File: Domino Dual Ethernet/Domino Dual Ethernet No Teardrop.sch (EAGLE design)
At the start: 21 parts, among them J1 MH10-1, J2 B50(27-51)FP4-151-A613-B12, J3 B50(27-51)FP4-151-A613-B12, J4 FR04-2, J5 FR04-1

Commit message: Changed copyright
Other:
- note added: "The Domino Team may make changes to specifications and product"
- note added: "© 2014, The Domino Team All rights reserved."
- note removed: "Michel Stempin may make changes to specifications and product"
- note removed: "© 2014, Michel Stempin All rights reserved."
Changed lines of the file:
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@@
 <text x="302.26" y="12.7" size="0.8128" layer="94">Reference designs are provided "AS IS" and "WITH ALL FAULTS".</text>
 <text x="302.26" y="10.16" size="0.8128" layer="94">regarding this product, including but not limited to, any implied warranties of</text>
-<text x="302.26" y="6.35" size="0.8128" layer="94">Michel Stempin may make changes to specifications and product </text>
+<text x="302.26" y="6.35" size="0.8128" layer="94">The Domino Team may make changes to specifications and product </text>
 <text x="302.26" y="11.43" size="0.8128" layer="94">Global Marine Networks disclaims all other warranties express or implied, </text>
 <text x="302.26" y="8.89" size="0.8128" layer="94">merchantibility or fitness for any particular application.</text>
@@
 <text x="256.54" y="7.62" size="1.778" layer="94" align="center">Domino
 Qi</text>
-<text x="345.44" y="20.32" size="1.27" layer="94">© 2014, Michel Stempin
+<text x="345.44" y="20.32" size="1.27" layer="94">© 2014, The Domino Team
 All rights reserved.</text>
 <text x="379.222" y="5.334" size="1.778" layer="94">&gt;REV</text>

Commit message: Domino tile Dual Ethernet Revision B
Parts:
- removed J4: FR04-2, Domino:FR04-2
- removed J5: FR04-1, Domino:FR04-1
- added D1: BLUE, Domino:LED_0603
- added D2: WHITE, Domino:LED_0603
- added D3, D4, D5, D6: GREEN, Domino:LED_0603
- added D7: RED, Domino:LED_0603
- added D8: ORANGE, Domino:LED_0603
- added D9: YELLOW, Domino:LED_0603
- added R10, R11, R12, R13, R15: 270R, Domino:RES_0603
- added R14, R16: 150R, Domino:RES_0603
- added R17, R18: 330R, Domino:RES_0603
- added R9: 49R9, Domino:RES_0402
- C1: device Domino:CAP_1210 -> Domino:CAP_1206
- J1: value MH10-1 -> B59(57-02)F4-03-1212-C12; device Domino:MH10-1 -> Domino:B59(57-02)F4-03-1212-C12; PARTNO MH10-1-0.1 -> B59(57-02)F4-03-1212-C12
- J2, J3: value B50(27-51)FP4-151-A613-B12 -> MH18-1; device Domino:B50(27-51)FP4-151-A613-B12 -> Domino:MH18-1; PARTNO B50(27-51)FP4-151-A613-B12 -> MH18-1-0.1
- R1: value 49R9 -> 330R; device Domino:RES_0402 -> Domino:RES_0603; PARTNO R0402_49R9_1%_62.5mW -> R0603_330R_5%_125mW; TOL 1% -> 5%
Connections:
- removed net P0_LED_L_A: J2.13, J4.8
- removed net P0_LED_L_C: J2.14, J4.7
- removed net P0_LED_R_A: J2.11, J4.4
- removed net P0_LED_R_C: J2.12, J4.3
- removed net P4_LED_L_A: J3.13, J4.6
- removed net P4_LED_L_C: J3.14, J4.5
- removed net P4_LED_R_A: J3.11, J4.2
- removed net P4_LED_R_C: J3.12, J4.1
- removed net VC12: J3.9, J5.3
- removed net VC36: J3.10, J5.4
- removed net VC45: J3.4, J5.1
- removed net VC78: J3.5, J5.2
- new net +3V3: D7.A, D8.A, D9.A, J1.UL2, J2.8, R1.2
- new net LAN1_LED: D3.A, R12.2
- new net LAN2_LED: D4.A, R13.2
- new net LAN3_LED: D5.A, J1.DL2, R14.2
- new net LAN4_LED: D6.A, R15.2
- new net LED0: J2.9, R10.1
- new net LED1: J2.10, R11.1
- new net LED2: J2.11, R12.1
- new net LED3: J2.12, R13.1
- new net LED4: J2.13, R14.1
- new net LED5: J2.14, R15.1
- new net LED6: J2.15, R16.1
- new net LED7: J2.16, R17.1
- new net LED8: J2.17, R18.1
- new net POWER_LED: J1.DL4, J1.UL4, R1.1
- new net SYS_LED: D8.C, R17.2
- new net USB_LED: D2.A, R11.2
- new net WAN_LED: D7.C, J1.UL1, R16.2
- new net WLAN_LED: D1.A, R10.2
- new net WPS_LED: D9.C, R18.2
- net +2VA_ETH_OUT: now also C2.2, C3.2, J1.DR2, J1.DR5, J1.UR2, J1.UR5, J3.14; no longer C6.2, C7.2, J1.6, J2.3, J3.3
- net GND: now also D1.C, D2.C, D3.C, D4.C, D5.C, D6.C, J1.DL1, J1.DL3, J1.UL3, J2.18, J3.9; no longer J1.1
- net P0_RX: now also C7.2, R8.1, R9.1; no longer C2.2, R1.1, R2.1
- net P0_RX_N: now also J1.DR3, J3.16, R9.2; no longer J1.8, J2.2, R2.2
- net P0_RX_P: now also J1.DR1, J3.15, R8.2; no longer J1.7, J2.1, R1.2
- net P0_TX: now also C6.2, R6.1, R7.1; no longer C3.2, R3.1, R4.1
- net P0_TX_N: now also J1.DR6, J3.18, R7.2; no longer J1.10, J2.8, R4.2
- net P0_TX_P: now also J1.DR4, J3.17, R6.2; no longer J1.9, J2.7, R3.2
- net P4_RX: now also C5.2, R4.1; no longer C4.2, R6.1
- net P4_RX_N: now also J1.UR6, J3.11, R5.2; no longer J1.3, J3.8, R6.2
- net P4_RX_P: now also J1.UR4, J3.10, R4.2; no longer J1.2, J3.7, R5.2
- net P4_TX: now also C4.2, R2.1, R3.1; no longer C5.2, R7.1, R8.1
- net P4_TX_N: now also J1.UR3, J3.13, R3.2; no longer J1.5, J3.2, R8.2
- net P4_TX_P: now also J1.UR1, J3.12, R2.2; no longer J1.4, J3.1, R7.2
- net SHIELD: now also J1.DR8, J1.SHIELD@1, J1.SHIELD@2, J1.SHIELD@3, J1.SHIELD@4, J1.UR8; no longer J2.6, J2.SHIELD@1, J2.SHIELD@2, J3.6, J3.SHIELD@1, J3.SHIELD@2
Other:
- note added: "LAN1"
- note added: "LAN2"
- note added: "LAN3"
- note added: "LAN4"
- note added: "SYS"
- note added: "USB"
- note added: "WAN"
- note added: "WLAN"
- note added: "WPS"
- note removed: "LEDS"
- note removed: "PoE"
- moved on the sheet: C1, C2, C3, C4, C5, C6, C7, R1, R2, R3, R4, R5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

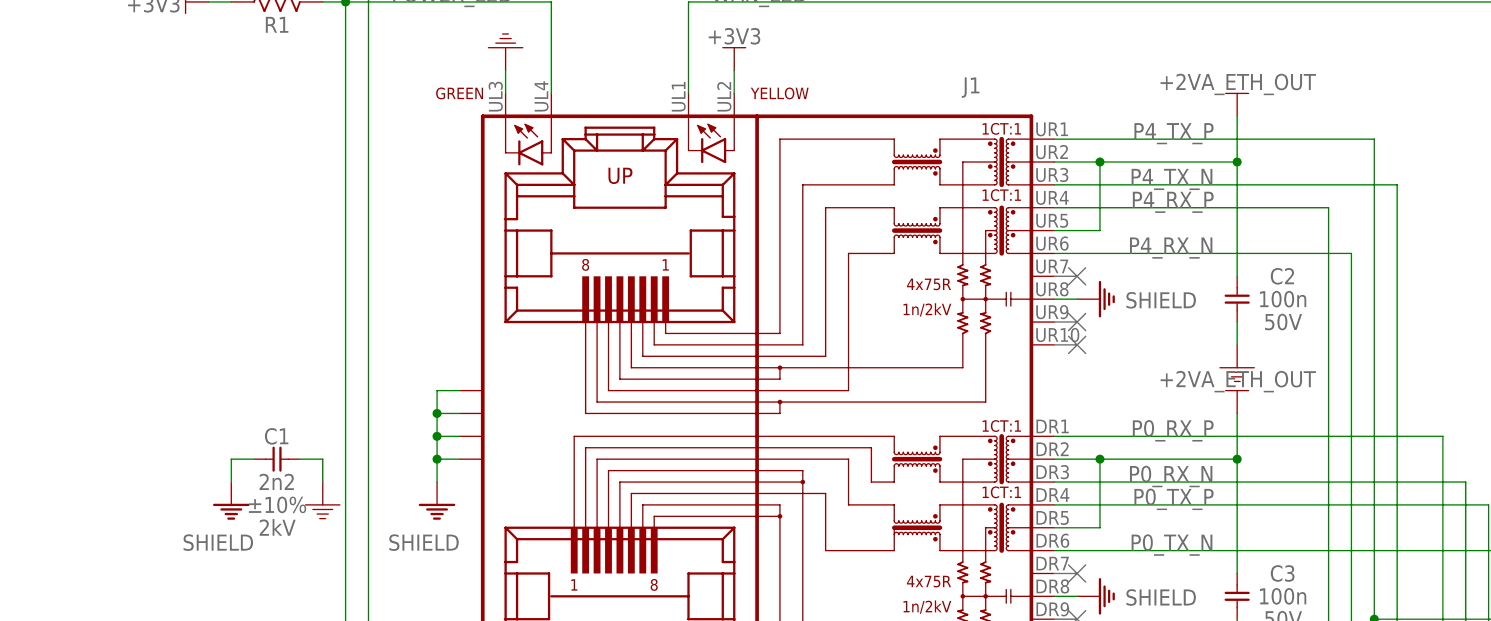
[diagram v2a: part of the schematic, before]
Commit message: Domino Single USB tile Revision B
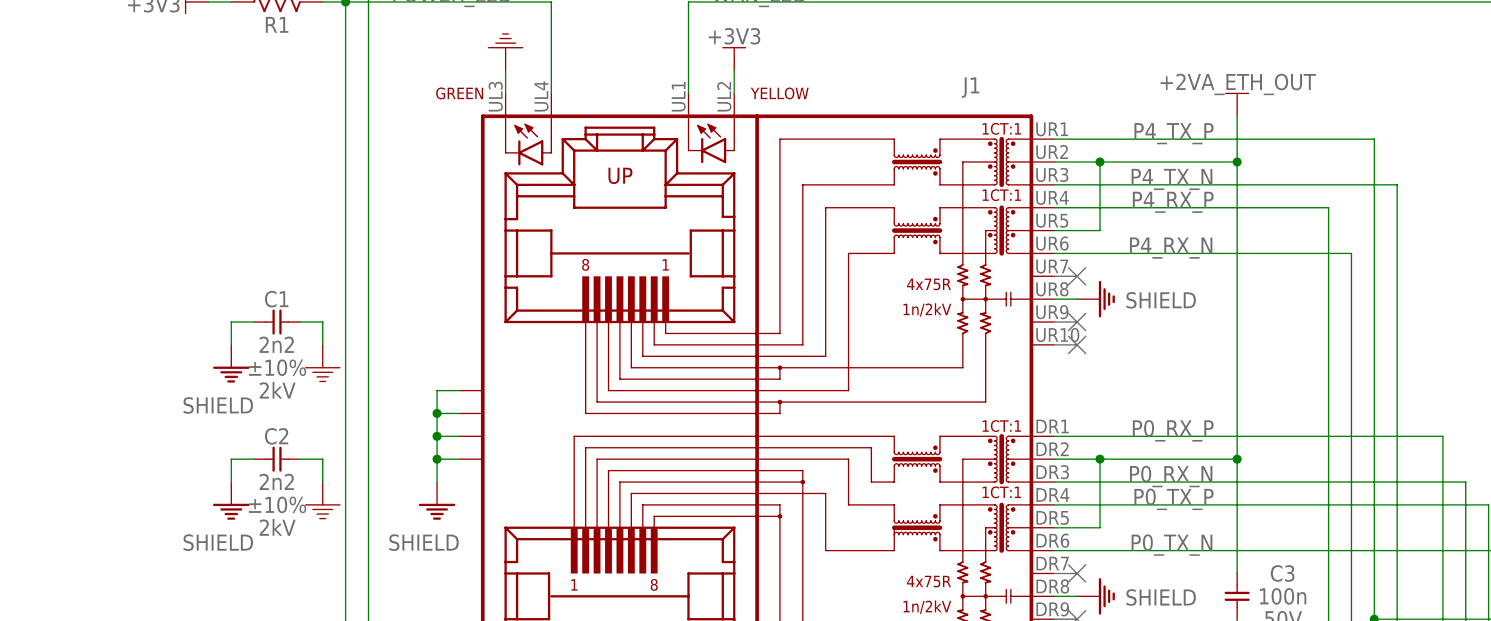
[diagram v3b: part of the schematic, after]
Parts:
- C2: value 100n -> 2n2; device Domino:CAP_0402 -> Domino:CAP_1206; PARTNO C0402_100n_X7R_10%_CER_50V -> C1210_2n2_X7R_10%_CER_2kV; VOLT 50V -> 2kV
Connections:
- net +2VA_ETH_OUT: no longer C2.2
- net SHIELD: now also C2.2
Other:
- moved on the sheet: C1, C2
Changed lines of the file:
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@@
 </part>
 <part name="SUPPLY2" library="Domino" deviceset="GND" device=""/>
-<part name="C2" library="Domino" deviceset="CAP_" device="0402" value="100n">
-<attribute name="PARTNO" value="C0402_100n_X7R_10%_CER_50V"/>
-<attribute name="TC" value="X7R"/>
-<attribute name="TOL" value="±10%"/>
-<attribute name="TYPE" value="CER"/>
-<attribute name="VOLT" value="50V"/>
-</part>
-<part name="SUPPLY5" library="Domino" deviceset="GND" device=""/>
 <part name="U$1" library="Domino" deviceset="+2VA_ETH_OUT" device=""/>
 <part name="SHIELD1" library="Domino" deviceset="SHIELD" device=""/>
@@
 </part>
 <part name="SUPPLY11" library="Domino" deviceset="GND" device=""/>
-<part name="U$19" library="Domino" deviceset="+2VA_ETH_OUT" device=""/>
 <part name="SHIELD2" library="Domino" deviceset="SHIELD" device=""/>
 <part name="PORT20" library="Domino" deviceset="NC" device=""/>
@@
 <part name="SUPPLY12" library="Domino" deviceset="GND" device=""/>
 <part name="SUPPLY13" library="Domino" deviceset="GND" device=""/>
+<part name="C2" library="Domino" deviceset="CAP_" device="1206" value="2n2">
+<attribute name="PARTNO" value="C1210_2n2_X7R_10%_CER_2kV"/>
+<attribute name="TC" value="X7R"/>
+<attribute name="TOL" value="±10%"/>
+<attribute name="TYPE" value="CER"/>
+<attribute name="VOLT" value="2kV"/>
+</part>
+<part name="SHIELD3" library="Domino" deviceset="SHIELD" device=""/>
+<part name="SUPPLY5" library="Domino" deviceset="GND" device=""/>
 </parts>
 <sheets>
@@
 </instance>
 <instance part="SUPPLY2" gate="GND" x="264.16" y="109.22" rot="MR0"/>
-<instance part="C2" gate="G$1" x="198.12" y="154.94" smashed="yes" rot="R90">
-<attribute name="VOLT" x="203.2" y="152.4" size="1.778" layer="96" rot="R180" align="center"/>
-<attribute name="PARTNO" x="198.12" y="154.94" size="1.778" layer="96" rot="R90" display="off"/>
-<attribute name="TC" x="198.12" y="154.94" size="1.778" layer="96" rot="R90" display="off"/>
-<attribute name="TOL" x="198.12" y="154.94" size="1.778" layer="96" rot="R90" display="off"/>
-<attribute name="TYPE" x="198.12" y="154.94" size="1.778" layer="96" rot="R90" display="off"/>
-<attribute name="NAME" x="203.2" y="157.48" size="1.778" layer="95" align="center"/>
-<attribute name="VALUE" x="203.2" y="154.94" size="1.778" layer="96" align="center"/>
-</instance>
-<instance part="SUPPLY5" gate="GND" x="198.12" y="149.86"/>
 <instance part="U$1" gate="G$1" x="198.12" y="175.26"/>
 <instance part="SHIELD1" gate="M" x="109.22" y="132.08" smashed="yes" rot="MR0">
@@
 </instance>
 <instance part="FRAME1" gate="G$1" x="0" y="0"/>
-<instance part="C1" gate="G$1" x="91.44" y="137.16" smashed="yes" rot="MR0">
-<attribute name="PARTNO" x="91.44" y="137.16" size="1.778" layer="96" rot="MR0" display="off"/>
-<attribute name="TC" x="91.44" y="137.16" size="1.778" layer="96" rot="MR0" display="off"/>
-<attribute name="TOL" x="91.44" y="132.08" size="1.778" layer="96" rot="MR0" align="center"/>
-<attribute name="TYPE" x="91.44" y="137.16" size="1.778" layer="96" rot="MR0" display="off"/>
-<attribute name="VOLT" x="91.44" y="129.54" size="1.778" layer="96" rot="MR0" align="center"/>
-<attribute name="NAME" x="91.44" y="139.7" size="1.778" layer="95" rot="MR180" align="center"/>
-<attribute name="VALUE" x="91.44" y="134.62" size="1.778" layer="96" rot="MR180" align="center"/>
-</instance>
-<instance part="SHIELD6" gate="M" x="86.36" y="132.08" smashed="yes" rot="MR0">
-<attribute name="VALUE" x="88.9" y="127" size="1.778" layer="96" rot="MR0"/>
-</instance>
-<instance part="SUPPLY7" gate="GND" x="96.52" y="134.62" rot="MR0"/>
+<instance part="C1" gate="G$1" x="91.44" y="152.4" smashed="yes" rot="MR0">
+<attribute name="PARTNO" x="91.44" y="152.4" size="1.778" layer="96" rot="MR0" display="off"/>
+<attribute name="TC" x="91.44" y="152.4" size="1.778" layer="96" rot="MR0" display="off"/>
+<attribute name="TOL" x="91.44" y="147.32" size="1.778" layer="96" rot="MR0" align="center"/>
+<attribute name="TYPE" x="91.44" y="152.4" size="1.778" layer="96" rot="MR0" display="off"/>
+<attribute name="VOLT" x="91.44" y="144.78" size="1.778" layer="96" rot="MR0" align="center"/>
+<attribute name="NAME" x="91.44" y="154.94" size="1.778" layer="95" rot="MR180" align="center"/>
+<attribute name="VALUE" x="91.44" y="149.86" size="1.778" layer="96" rot="MR180" align="center"/>
+</instance>
+<instance part="SHIELD6" gate="M" x="86.36" y="147.32" smashed="yes" rot="MR0">
+<attribute name="VALUE" x="88.9" y="142.24" size="1.778" layer="96" rot="MR0"/>
+</instance>
+<instance part="SUPPLY7" gate="GND" x="96.52" y="149.86" rot="MR0"/>
 <instance part="CC-BY-SA1" gate="G$1" x="269.24" y="10.16" smashed="yes"/>
 <instance part="PORT1" gate="G$1" x="203.2" y="40.64" rot="MR270"/>
@@
 </instance>
 <instance part="SUPPLY11" gate="GND" x="198.12" y="116.84"/>
-<instance part="U$19" gate="G$1" x="198.12" y="142.24"/>
 <instance part="SHIELD2" gate="M" x="182.88" y="121.92" smashed="yes" rot="MR270">
 <attribute name="VALUE" x="185.674" y="122.682" size="1.778" layer="96" rot="MR180"/>
@@
 <instance part="SUPPLY12" gate="GND" x="116.84" y="101.6"/>
 <instance part="SUPPLY13" gate="GND" x="137.16" y="101.6"/>
+<instance part="C2" gate="G$1" x="91.44" y="137.16" smashed="yes" rot="MR0">
+<attribute name="PARTNO" x="91.44" y="137.16" size="1.778" layer="96" rot="MR0" display="off"/>
+<attribute name="TC" x="91.44" y="137.16" size="1.778" layer="96" rot="MR0" display="off"/>
+<attribute name="TOL" x="91.44" y="132.08" size="1.778" layer="96" rot="MR0" align="center"/>
+<attribute name="TYPE" x="91.44" y="137.16" size="1.778" layer="96" rot="MR0" display="off"/>
+<attribute name="VOLT" x="91.44" y="129.54" size="1.778" layer="96" rot="MR0" align="center"/>
+<attribute name="NAME" x="91.44" y="139.7" size="1.778" layer="95" rot="MR180" align="center"/>
+<attribute name="VALUE" x="91.44" y="134.62" size="1.778" layer="96" rot="MR180" align="center"/>
+</instance>
+<instance part="SHIELD3" gate="M" x="86.36" y="132.08" smashed="yes" rot="MR0">
+<attribute name="VALUE" x="88.9" y="127" size="1.778" layer="96" rot="MR0"/>
+</instance>
+<instance part="SUPPLY5" gate="GND" x="96.52" y="134.62" rot="MR0"/>
 </instances>
 <busses>
@@
 </segment>
 <segment>
-<pinref part="C2" gate="G$1" pin="1"/>
-<pinref part="SUPPLY5" gate="GND" pin="GND"/>
-<wire x1="198.12" y1="152.4" x2="198.12" y2="149.86" width="0.1524" layer="91"/>
-</segment>
-<segment>
 <pinref part="C1" gate="G$1" pin="1"/>
 <pinref part="SUPPLY7" gate="GND" pin="GND"/>
-<wire x1="93.98" y1="137.16" x2="96.52" y2="137.16" width="0.1524" layer="91"/>
-<wire x1="96.52" y1="137.16" x2="96.52" y2="134.62" width="0.1524" layer="91"/>
+<wire x1="93.98" y1="152.4" x2="96.52" y2="152.4" width="0.1524" layer="91"/>
+<wire x1="96.52" y1="152.4" x2="96.52" y2="149.86" width="0.1524" layer="91"/>
 </segment>
 <segment>
@@
 <wire x1="137.16" y1="101.6" x2="137.16" y2="104.14" width="0.1524" layer="91"/>
 </segment>
+<segment>
+<pinref part="C2" gate="G$1" pin="1"/>
+<pinref part="SUPPLY5" gate="GND" pin="GND"/>
+<wire x1="93.98" y1="137.16" x2="96.52" y2="137.16" width="0.1524" layer="91"/>
+<wire x1="96.52" y1="137.16" x2="96.52" y2="134.62" width="0.1524" layer="91"/>
+</segment>
 </net>
 <net name="P4_TX" class="0">
@@
 <segment>
 <pinref part="U$1" gate="G$1" pin="+2VA_ETH_OUT"/>
-<pinref part="C2" gate="G$1" pin="2"/>
 <wire x1="198.12" y1="175.26" x2="198.12" y2="170.18" width="0.1524" layer="91"/>
-<wire x1="198.12" y1="170.18" x2="198.12" y2="157.48" width="0.1524" layer="91"/>
-<junction x="198.12" y="170.18"/>
 <wire x1="198.12" y1="170.18" x2="182.88" y2="170.18" width="0.1524" layer="91"/>
 <wire x1="182.88" y1="170.18" x2="177.8" y2="170.18" width="0.1524" layer="91"/>
@@
 <pinref part="J1" gate="G$1" pin="UR2"/>
 <pinref part="J1" gate="G$1" pin="UR5"/>
-</segment>
-<segment>
-<wire x1="218.44" y1="40.64" x2="218.44" y2="38.1" width="0.1524" layer="91"/>
-<pinref part="J3" gate="G$1" pin="14"/>
-<pinref part="U$20" gate="G$1" pin="+2VA_ETH_OUT"/>
-</segment>
-<segment>
-<pinref part="U$19" gate="G$1" pin="+2VA_ETH_OUT"/>
 <pinref part="C3" gate="G$1" pin="2"/>
-<wire x1="198.12" y1="142.24" x2="198.12" y2="137.16" width="0.1524" layer="91"/>
 <wire x1="198.12" y1="137.16" x2="198.12" y2="124.46" width="0.1524" layer="91"/>
-<junction x="198.12" y="137.16"/>
 <wire x1="198.12" y1="137.16" x2="182.88" y2="137.16" width="0.1524" layer="91"/>
 <wire x1="182.88" y1="137.16" x2="177.8" y2="137.16" width="0.1524" layer="91"/>
@@
 <pinref part="J1" gate="G$1" pin="DR2"/>
 <pinref part="J1" gate="G$1" pin="DR5"/>
+<wire x1="198.12" y1="170.18" x2="198.12" y2="137.16" width="0.1524" layer="91"/>
+<junction x="198.12" y="170.18"/>
+<junction x="198.12" y="137.16"/>
+</segment>
+<segment>
+<wire x1="218.44" y1="40.64" x2="218.44" y2="38.1" width="0.1524" layer="91"/>
+<pinref part="J3" gate="G$1" pin="14"/>
+<pinref part="U$20" gate="G$1" pin="+2VA_ETH_OUT"/>
 </segment>
 </net>
@@
 <pinref part="C1" gate="G$1" pin="2"/>
 <pinref part="SHIELD6" gate="M" pin="SHIELD"/>
-<wire x1="88.9" y1="137.16" x2="86.36" y2="137.16" width="0.1524" layer="91"/>
-<wire x1="86.36" y1="137.16" x2="86.36" y2="134.62" width="0.1524" layer="91"/>
+<wire x1="88.9" y1="152.4" x2="86.36" y2="152.4" width="0.1524" layer="91"/>
+<wire x1="86.36" y1="152.4" x2="86.36" y2="149.86" width="0.1524" layer="91"/>
 </segment>
 <segment>
@@
 <pinref part="J1" gate="G$1" pin="SHIELD@4"/>
 </segment>
+<segment>
+<pinref part="C2" gate="G$1" pin="2"/>
+<pinref part="SHIELD3" gate="M" pin="SHIELD"/>
+<wire x1="88.9" y1="137.16" x2="86.36" y2="137.16" width="0.1524" layer="91"/>
+<wire x1="86.36" y1="137.16" x2="86.36" y2="134.62" width="0.1524" layer="91"/>
+</segment>
 </net>
